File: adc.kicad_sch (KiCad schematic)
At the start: 8 parts, among them U1 AD4111BCPZ

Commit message: Launchpad controller revision 06/03/2024
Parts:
- renumbered C3 to C33, C1 to C34, C4 to C35, C5 to C36, C38 to C37, C2 to C38, C2 to C39, U1 to U6

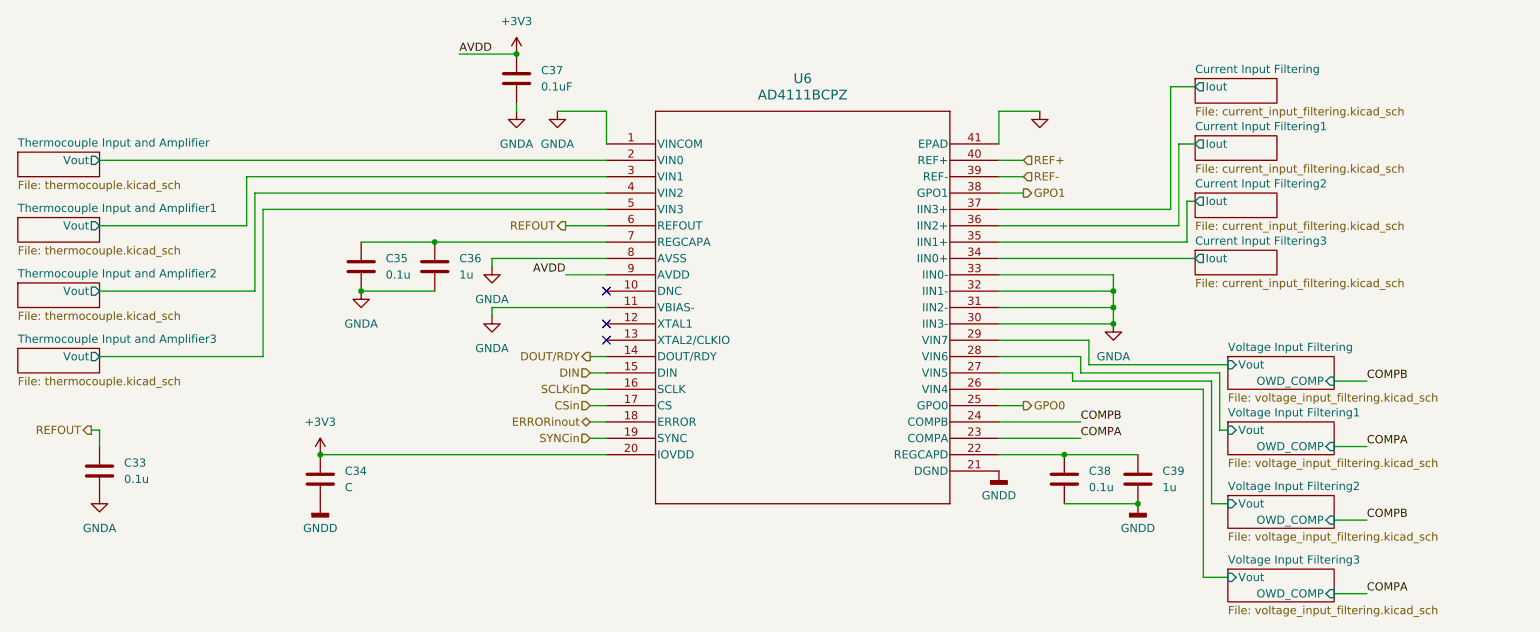
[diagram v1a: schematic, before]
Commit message: added footprints to almost all components
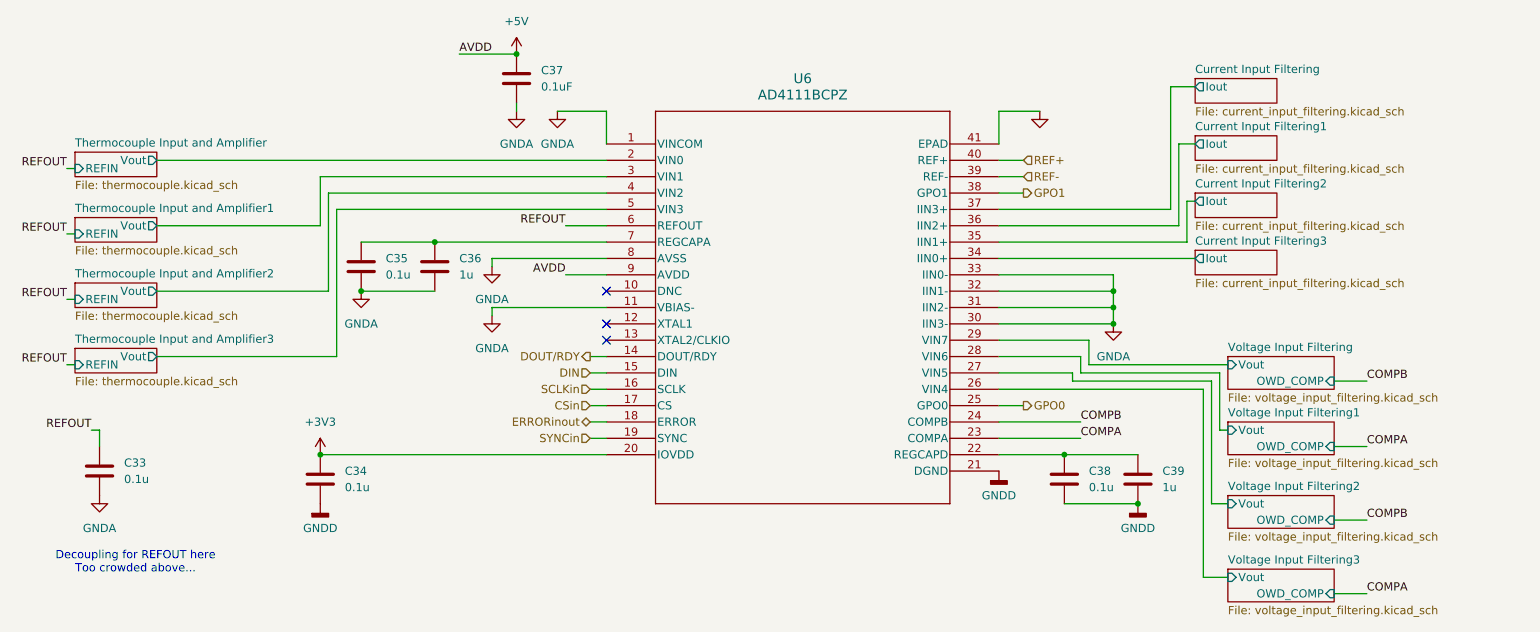
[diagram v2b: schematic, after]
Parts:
- C33, C35, C36, C37, C38, C39: footprint (none) -> Capacitor_SMD:C_0603_1608Metric_Pad1.08x0.95mm_HandSolder
- C34: value C -> 0.1u; footprint (none) -> Capacitor_SMD:C_0603_1608Metric_Pad1.08x0.95mm_HandSolder
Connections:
- net +3V3: no longer C37.1, U6.9 (AVDD)
- new net +5V: C37.1, U6.9 (AVDD)
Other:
- sheet Thermocouple Input and Amplifier ports: added REFIN; removed none
- sheet Thermocouple Input and Amplifier1 ports: added REFIN; removed none
- sheet Thermocouple Input and Amplifier2 ports: added REFIN; removed none
- sheet Thermocouple Input and Amplifier3 ports: added REFIN; removed none
- note added: "Decoupling for REFOUT here Too crowded above..."
